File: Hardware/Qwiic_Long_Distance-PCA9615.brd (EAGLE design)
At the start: 48.3 x 25.4 mm, 34 parts, among them J3 RJ45_RJ11_COMBO, U1 PCA9615

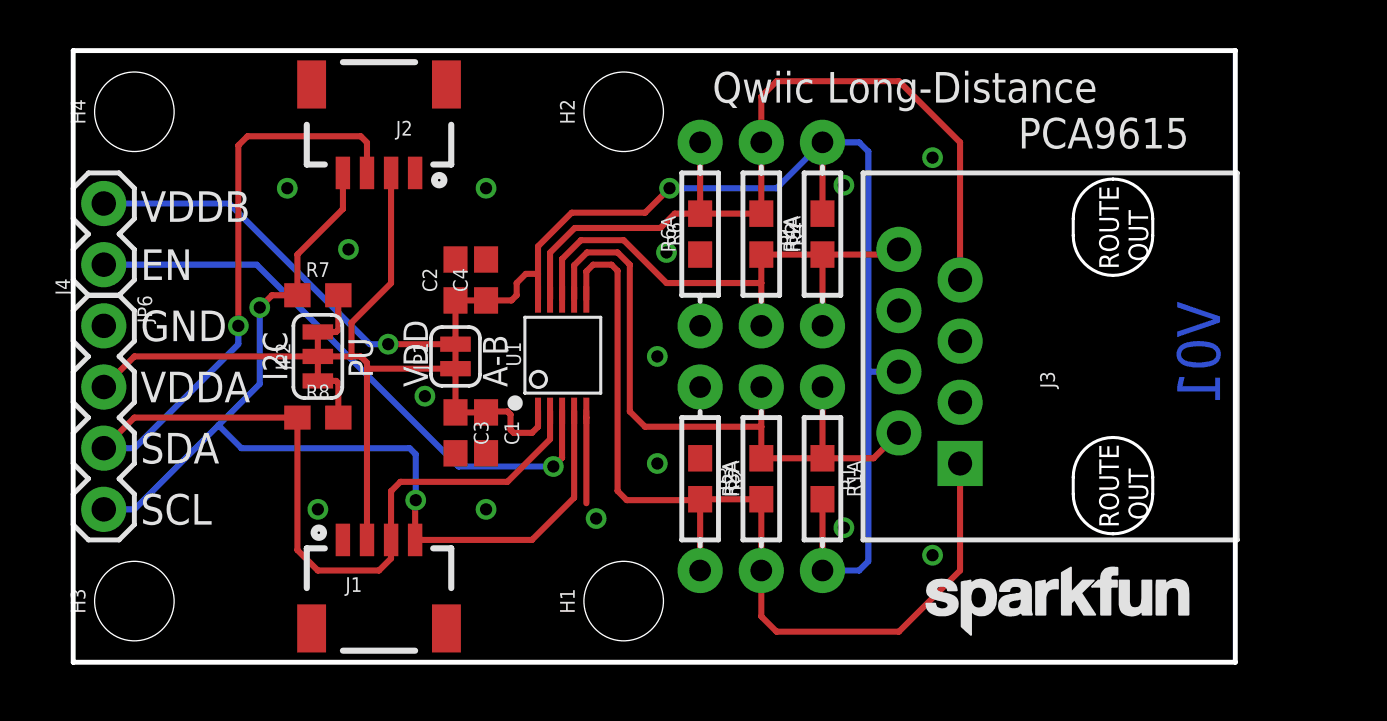
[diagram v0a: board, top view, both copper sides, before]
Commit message: Updated routing for Differential signals
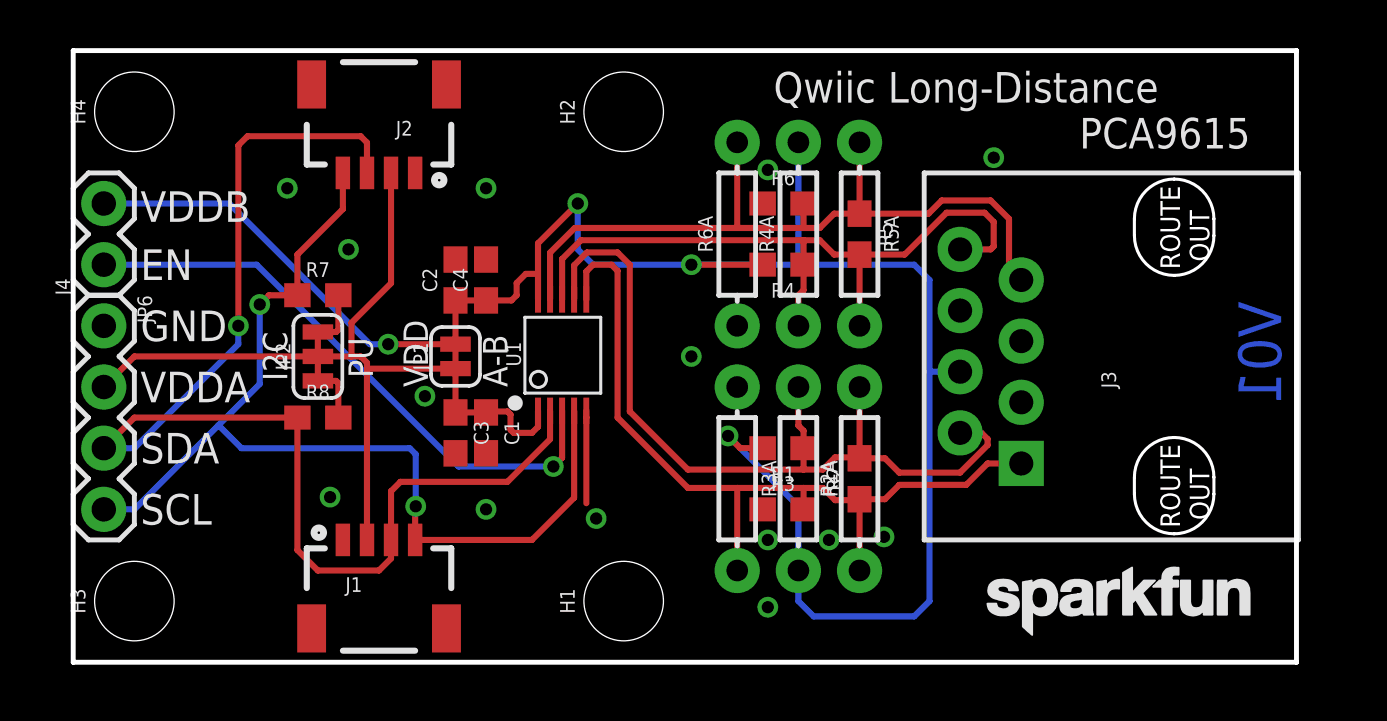
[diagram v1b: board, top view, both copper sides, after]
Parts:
- moved R2 4.08 mm to (32.7, 7.62)
- moved R2A 4.08 mm to (32.7, 7.62)
- moved R5 4.08 mm to (32.7, 17.8)
- moved R5A 4.08 mm to (32.7, 17.8)
- moved R3 3.67 mm to (29.5, 6.35), turned to 0 degrees
- moved R6 3.67 mm to (29.5, 19.1), turned to 0 degrees
- moved LOGO2 2.54 mm to (37.5, 0.64)
- moved J3 2.54 mm to (45.7, 12.7)
- moved LOGO1 2.54 mm to (45.7, 12.7)
- moved R1 2.07 mm to (29.5, 8.89), turned to 180 degrees
- moved R4 2.07 mm to (29.5, 16.5), turned to 180 degrees
- moved R3A 1.54 mm to (27.6, 7.62)
- moved R6A 1.54 mm to (27.6, 17.8)
- moved R1A 1.00 mm to (30.1, 7.62)
- moved R4A 1.00 mm to (30.1, 17.8)
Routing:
- net VDD_B: track 67.5 -> 83.4 mm, vias 2 -> 4
- net DSDA+: track 22.7 -> 30.1 mm
- net DSCL+: track 28.1 -> 35.0 mm
- net DSCL-: track 39.8 -> 34.9 mm
- net DSDA-: track 34.5 -> 32.5 mm
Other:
- board size 48.3 x 25.4 mm -> 50.8 x 25.4 mm

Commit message: ENG Checklist update
Changes made after design review and ENG checklist.
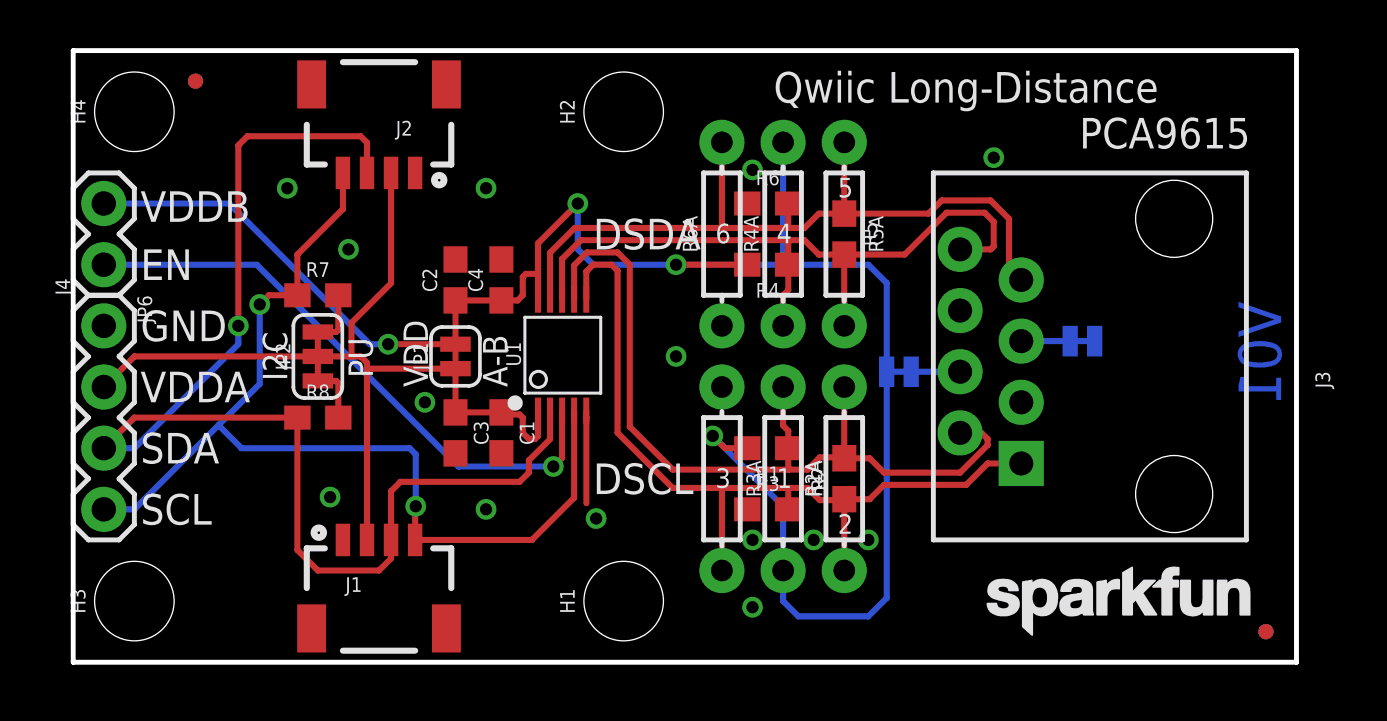
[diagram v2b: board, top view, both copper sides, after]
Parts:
- added FD1, FD2, FD3, FD4: FIDUCIALUFIDUCIAL, SparkFun-Aesthetics:FIDUCIAL-MICRO
- added JP3, JP4: (no value), SparkFun-Jumpers:SMT-JUMPER_2_NC_TRACE_SILK
- J3: value RJ45_RJ11_COMBO -> RJ45; device SparkX:RJ45_RJ11_COMBO -> SparkFun-Connectors:RJ45-8
- moved C1 0.64 mm to (17.8, 9.53)
- moved C4 0.64 mm to (17.8, 15.9)
- moved R1 0.64 mm to (28.8, 8.89)
- moved R3 0.64 mm to (28.8, 6.35)
- moved R4 0.64 mm to (28.8, 16.5)
- moved R6 0.64 mm to (28.8, 19.1)
- moved R1A 0.63 mm to (29.5, 7.62)
- moved R2 0.63 mm to (32.0, 7.62)
- moved R2A 0.63 mm to (32.0, 7.62)
- moved R3A 0.63 mm to (26.9, 7.62)
- moved R4A 0.63 mm to (29.5, 17.8)
- moved R5 0.63 mm to (32.0, 17.8)
- moved R5A 0.63 mm to (32.0, 17.8)
- moved R6A 0.63 mm to (26.9, 17.8)
- moved LOGO1 0.25 mm to (46.0, 12.7)
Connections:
- new net N$1: J3.4, JP3.2
- new net N$2: J3.5, JP4.2
- net GND: now also JP4.1; no longer J3.5
- net VDD_B: now also JP3.1; no longer J3.4
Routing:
- net VDD_B: track 83.4 -> 79.2 mm
- net N$2: track 0.00 -> 2.03 mm
- net N$1: track 0.00 -> 2.03 mm
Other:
- board text added: "1"
- board text added: "2"
- board text added: "3"
- board text added: "4"
- board text added: "5"
- board text added: "6"
- board text added: "DSCL"
- board text added: "DSDA"

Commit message: Adding minor changes from QC checklist
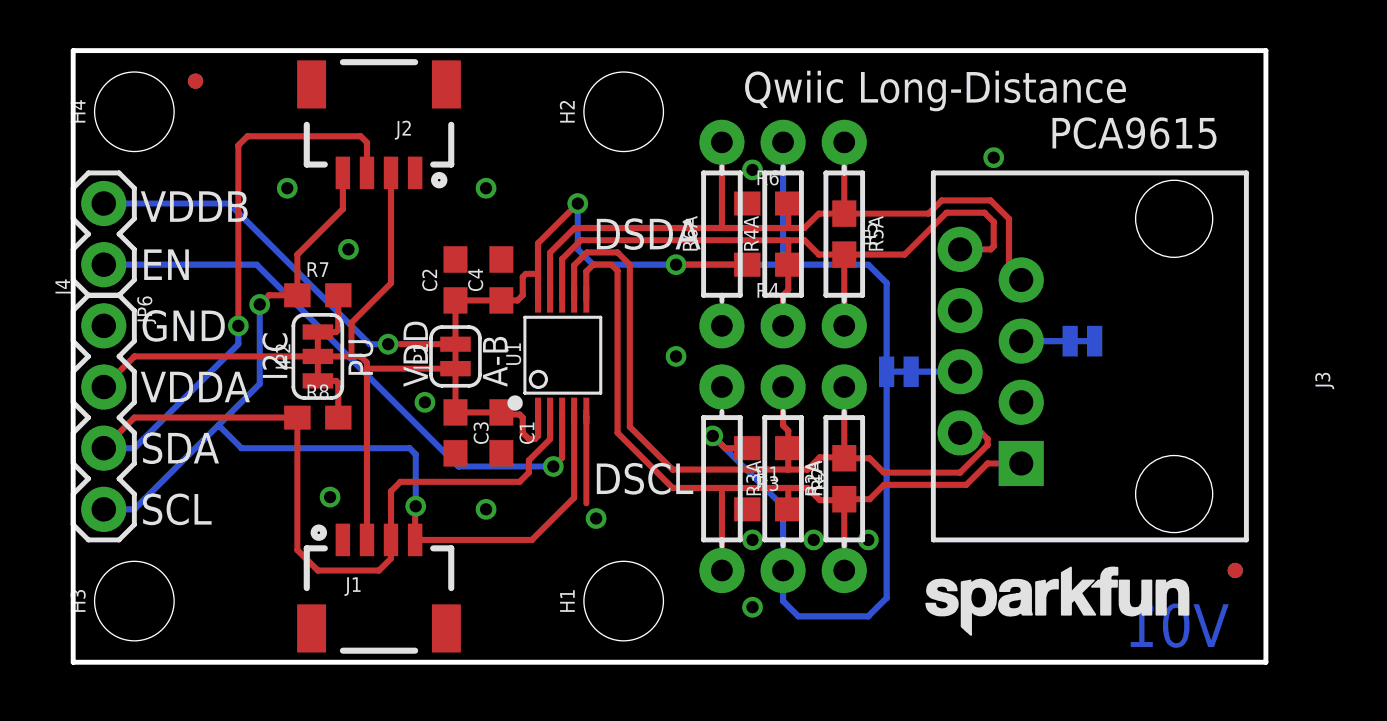
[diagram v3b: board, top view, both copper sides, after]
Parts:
- removed LOGO3: SFE_LOGO_NAME.1_INCH, SparkFun-Aesthetics:SFE_LOGO_NAME_.1
- added LOGO5: SFE_LOGO_NAME_FLAME.1_INCH, SparkFun-Aesthetics:SFE_LOGO_NAME_FLAME_.1
- moved FD2 2.84 mm to (48.3, 3.81)
- moved FD4 2.84 mm to (48.3, 3.81)
- moved LOGO2 2.54 mm to (34.9, 0.64)
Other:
- board size 50.8 x 25.4 mm -> 49.5 x 25.4 mm
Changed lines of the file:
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@@
 <setting verticaltext="up"/>
 </settings>
-<grid distance="0.025" unitdist="inch" unit="inch" style="lines" multiple="1" display="yes" altdistance="0.005" altunitdist="inch" altunit="inch"/>
+<grid distance="0.05" unitdist="inch" unit="inch" style="lines" multiple="1" display="yes" altdistance="0.005" altunitdist="inch" altunit="inch"/>
 <layers>
 <layer number="1" name="Top" color="4" fill="1" visible="yes" active="yes"/>
@@
 <layer number="45" name="Holes" color="7" fill="1" visible="yes" active="yes"/>
 <layer number="46" name="Milling" color="3" fill="1" visible="no" active="yes"/>
-<layer number="47" name="Measures" color="7" fill="1" visible="yes" active="yes"/>
+<layer number="47" name="Measures" color="7" fill="1" visible="no" active="yes"/>
 <layer number="48" name="Document" color="7" fill="1" visible="no" active="yes"/>
 <layer number="49" name="Reference" color="7" fill="1" visible="yes" active="yes"/>
@@
 <text x="2.794" y="15.875" size="1.27" layer="21" font="vector" ratio="15" rot="SR0">EN</text>
 <text x="2.794" y="18.288" size="1.27" layer="21" font="vector" ratio="15" rot="SR0">VDDB</text>
-<wire x1="50.8" y1="0" x2="0" y2="0" width="0.2032" layer="20"/>
+<wire x1="49.53" y1="0" x2="0" y2="0" width="0.2032" layer="20"/>
 <wire x1="0" y1="0" x2="0" y2="25.4" width="0.2032" layer="20"/>
-<wire x1="0" y1="25.4" x2="50.8" y2="25.4" width="0.2032" layer="20"/>
-<wire x1="50.8" y1="25.4" x2="50.8" y2="0" width="0.2032" layer="20"/>
+<wire x1="0" y1="25.4" x2="49.53" y2="25.4" width="0.2032" layer="20"/>
+<wire x1="49.53" y1="25.4" x2="49.53" y2="0" width="0.2032" layer="20"/>
 <text x="1.27" y="20.32" size="1.778" layer="47">Measurements in mm</text>
-<text x="29.083" y="23.241" size="1.27" layer="21" font="vector" ratio="15">Qwiic Long-Distance </text>
+<text x="27.813" y="23.241" size="1.27" layer="21" font="vector" ratio="15">Qwiic Long-Distance </text>
 <text x="8.89" y="11.684" size="1.016" layer="21" font="vector" ratio="15" rot="R90">I2C</text>
 <text x="12.446" y="11.811" size="1.016" layer="21" font="vector" ratio="15" rot="R90">PU</text>
 <text x="14.732" y="11.43" size="1.016" layer="21" font="vector" ratio="15" rot="R90">VDD</text>
 <text x="18.034" y="11.43" size="1.016" layer="21" font="vector" ratio="15" rot="R90">A-B</text>
-<text x="7.239" y="18.288" size="1.27" layer="22" font="vector" ratio="15" rot="SMR0">VDDB</text>
+<text x="7.1755" y="18.415" size="1.27" layer="22" font="vector" ratio="15" rot="SMR0">VDDB</text>
 <text x="4.8895" y="15.875" size="1.27" layer="22" font="vector" ratio="15" rot="SMR0">EN</text>
 <text x="6.0325" y="13.335" size="1.27" layer="22" font="vector" ratio="15" rot="SMR0">GND</text>
@@
 <text x="6.0325" y="8.255" size="1.27" layer="22" font="vector" ratio="15" rot="SMR0">SDA</text>
 <text x="6.0325" y="5.715" size="1.27" layer="22" font="vector" ratio="15" rot="SMR0">SCL</text>
-<text x="49.657" y="23.241" size="1.27" layer="22" font="vector" ratio="15" rot="MR0">Qwiic Long-Distance</text>
+<text x="48.387" y="23.241" size="1.27" layer="22" font="vector" ratio="15" rot="MR0">Qwiic Long-Distance</text>
 <text x="39.751" y="6.7945" size="0.8128" layer="22" font="vector" ratio="15" rot="SMR270">DSCL-</text>
 <text x="37.211" y="8.128" size="0.8128" layer="22" font="vector" ratio="15" rot="SMR270">DSCL+</text>
@@
 <wire x1="38.1635" y1="7.0485" x2="38.1635" y2="9.4615" width="0.254" layer="22"/>
 <text x="42.291" y="16.637" size="0.8128" layer="22" font="vector" ratio="15" rot="SMR270">GND</text>
-<text x="35.1155" y="16.129" size="0.8128" layer="22" font="vector" ratio="15" rot="SMR270">VDDB</text>
+<text x="34.6964" y="16.0655" size="0.8128" layer="22" font="vector" ratio="15" rot="SMR270">VDDB</text>
 <circle x="36.83" y="12.065" radius="1.1447625" width="0.254" layer="22"/>
 <circle x="39.37" y="13.335" radius="1.1447625" width="0.254" layer="22"/>
-<text x="41.783" y="21.336" size="1.27" layer="21" font="vector" ratio="15">PCA9615</text>
-<text x="49.657" y="21.336" size="1.27" layer="22" font="vector" ratio="15" rot="MR0">PCA9615</text>
-<text x="50.165" y="14.986" size="1.778" layer="16" font="vector" ratio="15" rot="SMR270">V01</text>
+<text x="40.513" y="21.336" size="1.27" layer="21" font="vector" ratio="15">PCA9615</text>
+<text x="48.387" y="21.336" size="1.27" layer="22" font="vector" ratio="15" rot="MR0">PCA9615</text>
+<text x="48.006" y="0.635" size="1.778" layer="16" font="vector" ratio="15" rot="SMR0">V01</text>
 <text x="21.59" y="17.145" size="1.27" layer="21" font="vector" ratio="15">DSDA</text>
 <text x="21.59" y="6.985" size="1.27" layer="21" font="vector" ratio="15">DSCL</text>
-<text x="31.75" y="5.334" size="0.8128" layer="21" font="vector" ratio="15">2</text>
-<text x="26.67" y="7.239" size="0.8128" layer="21" font="vector" ratio="15">3</text>
-<text x="29.21" y="7.239" size="0.8128" layer="21" font="vector" ratio="15">1</text>
-<text x="29.21" y="17.399" size="0.8128" layer="21" font="vector" ratio="15">4</text>
-<text x="31.75" y="19.304" size="0.8128" layer="21" font="vector" ratio="15">5</text>
-<text x="26.67" y="17.399" size="0.8128" layer="21" font="vector" ratio="15">6</text>
 <wire x1="32.766" y1="15.24" x2="32.766" y2="20.32" width="0.254" layer="22"/>
 <wire x1="32.766" y1="20.32" x2="31.242" y2="20.32" width="0.254" layer="22"/>
@@
 <element name="H4" library="SparkFun-Hardware" package="STAND-OFF" value="STAND-OFF" x="2.54" y="22.86" rot="R90"/>
 <element name="J4" library="SparkFun-Connectors" package="1X02" value="" x="1.27" y="16.51" rot="R90"/>
-<element name="LOGO2" library="SparkFun-Aesthetics" package="SFE_LOGO_NAME_.1" value="SFE_LOGO_NAME.1_INCH" x="37.465" y="0.635"/>
+<element name="LOGO2" library="SparkFun-Aesthetics" package="SFE_LOGO_NAME_.1" value="SFE_LOGO_NAME.1_INCH" x="34.925" y="0.635"/>
 <element name="LOGO1" library="SparkFun-Aesthetics" package="OSHW-LOGO-M" value="OSHW-LOGOM" x="45.974" y="12.7" rot="MR270"/>
-<element name="LOGO3" library="SparkFun-Aesthetics" package="SFE_LOGO_NAME_.1" value="SFE_LOGO_NAME.1_INCH" x="19.05" y="0.635" rot="MR0"/>
 <element name="JP3" library="SparkFun-Jumpers" package="SMT-JUMPER_2_NC_TRACE_SILK" value="" x="34.29" y="12.065" rot="MR180"/>
 <element name="JP4" library="SparkFun-Jumpers" package="SMT-JUMPER_2_NC_TRACE_SILK" value="" x="41.91" y="13.335" rot="MR0"/>
 <element name="FD1" library="SparkFun-Aesthetics" package="FIDUCIAL-MICRO" value="FIDUCIALUFIDUCIAL" x="5.08" y="24.13"/>
-<element name="FD2" library="SparkFun-Aesthetics" package="FIDUCIAL-MICRO" value="FIDUCIALUFIDUCIAL" x="49.53" y="1.27"/>
+<element name="FD2" library="SparkFun-Aesthetics" package="FIDUCIAL-MICRO" value="FIDUCIALUFIDUCIAL" x="48.26" y="3.81"/>
 <element name="FD3" library="SparkFun-Aesthetics" package="FIDUCIAL-MICRO" value="FIDUCIALUFIDUCIAL" x="5.08" y="24.13" rot="MR0"/>
-<element name="FD4" library="SparkFun-Aesthetics" package="FIDUCIAL-MICRO" value="FIDUCIALUFIDUCIAL" x="49.53" y="1.27" rot="MR0"/>
+<element name="FD4" library="SparkFun-Aesthetics" package="FIDUCIAL-MICRO" value="FIDUCIALUFIDUCIAL" x="48.26" y="3.81" rot="MR0"/>
+<element name="LOGO5" library="SparkFun-Aesthetics" package="SFE_LOGO_NAME_FLAME_.1" value="SFE_LOGO_NAME_FLAME.1_INCH" x="18.415" y="0.762" rot="MR0"/>
 </elements>
 <signals>
@@
 <contactref element="JP6" pad="1"/>
 <polygon width="0.254" layer="1" isolate="0.3048">
-<vertex x="50.8" y="0"/>
+<vertex x="49.53" y="0"/>
 <vertex x="0" y="0"/>
 <vertex x="0" y="25.4"/>
-<vertex x="50.8" y="25.4"/>
+<vertex x="49.53" y="25.4"/>
 </polygon>
 <polygon width="0.254" layer="16" isolate="0.3048">
-<vertex x="50.8" y="0"/>
+<vertex x="49.53" y="0"/>
 <vertex x="0" y="0"/>
 <vertex x="0" y="25.4"/>
-<vertex x="50.8" y="25.4"/>
+<vertex x="49.53" y="25.4"/>
 </polygon>
 <via x="14.605" y="10.795" extent="1-16" drill="0.508"/>
